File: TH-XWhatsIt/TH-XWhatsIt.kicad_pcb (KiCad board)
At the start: 2 copper layers, 162.2 x 18.8 mm, 24 parts, among them J1 BEAMSPRING CONNECTOR, J3 EXPANSION HEADER, U1 MCP4921-EP, U2 LM339, U3 74HCT595, U4 74HCT595, U5 ProMicro, U7 74HCT595

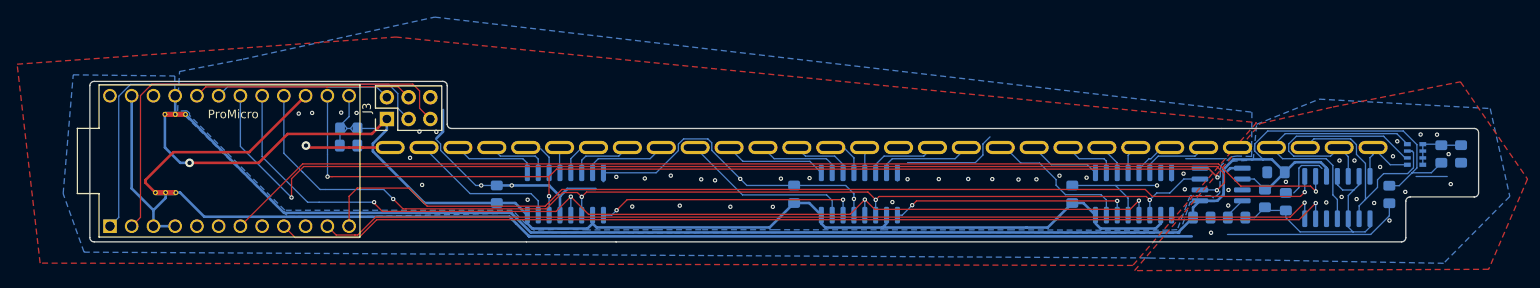
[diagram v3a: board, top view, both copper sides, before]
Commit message: cleaned up cuts in the copper fill
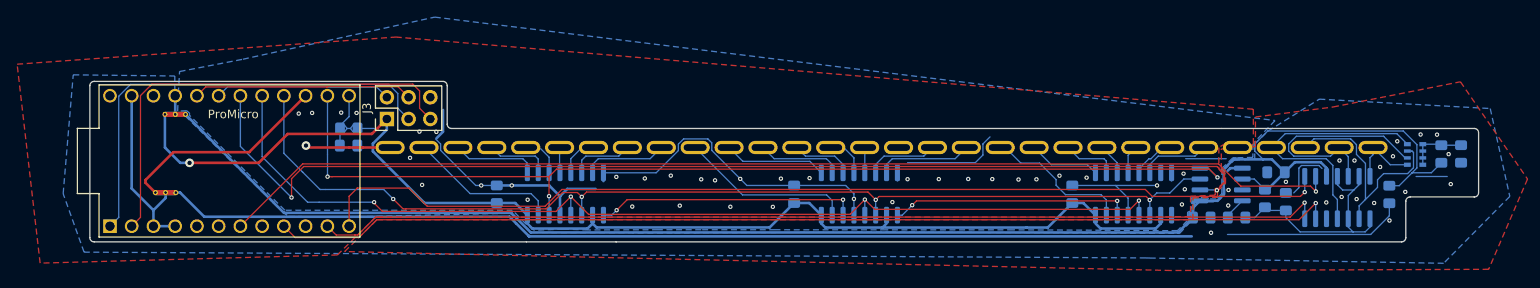
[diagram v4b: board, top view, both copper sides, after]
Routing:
- net GNDD: vias 37 -> 38
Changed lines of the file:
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@@
     (thickness 1.6)
     (drawings 20)
-    (tracks 554)
+    (tracks 555)
     (zones 0)
     (modules 24)
@@
   (layers
     (0 F.Cu jumper)
-    (31 B.Cu signal)
+    (31 B.Cu signal hide)
     (32 B.Adhes user hide)
     (33 F.Adhes user hide)
@@
     (42 Eco1.User user hide)
     (43 Eco2.User user hide)
-    (44 Edge.Cuts user hide)
+    (44 Edge.Cuts user)
     (45 Margin user hide)
     (46 B.CrtYd user hide)
@@
   (segment (start 100 153.84556) (end 100 153.524) (width 0.3048) (layer F.Cu) (net 56))
   (segment (start 101.15184 154.9974) (end 100 153.84556) (width 0.3048) (layer F.Cu) (net 56))
+  (via (at 221.09 156.38) (size 0.508) (drill 0.254) (layers F.Cu B.Cu) (net 56))
   (segment (start 103.4669 158.91662) (end 100.9269 158.91662) (width 0.3048) (layer B.Cu) (net 57))
   (segment (start 100.9269 158.91662) (end 100.9269 157.04718) (width 0.3048) (layer B.Cu) (net 57))
@@
         (xy 103.42118 141.36878) (xy 103.44404 146.00936) (xy 104.65054 146.03476) (xy 115.97386 157.22346) (xy 116.72824 157.78226)
         (xy 123.65482 157.8356) (xy 142.61084 157.4038) (xy 145.16862 159.67202) (xy 161.78276 159.70758) (xy 186.9694 159.6009)
-        (xy 220.81744 159.76092) (xy 222.0595 156.0703) (xy 225.10242 156.03474) (xy 225.8949 155.28036) (xy 225.94824 152.41778)
-        (xy 226.90328 151.33574) (xy 229.42296 151.1935) (xy 229.8192 147.0152) (xy 237.1471 144.07388) (xy 257.1115 145.17116)
-        (xy 259.3975 155.43784) (xy 251.67082 163.25088) (xy 217.42908 162.64128) (xy 216.86012 162.62604) (xy 92.8243 161.9504)
-        (xy 90.38082 155.12288) (xy 91.55684 141.23416)
+        (xy 220.81744 159.76092) (xy 222.25 158.232899) (xy 222.5 156.75442) (xy 223 156.0703) (xy 225.22 156.07)
+        (xy 226.1 155.23) (xy 226.08 152.31) (xy 227.19 151.2) (xy 229.6 151.12) (xy 229.6 149.31)
+        (xy 231.14 147.81) (xy 237.1471 144.07388) (xy 257.1115 145.17116) (xy 259.3975 155.43784) (xy 251.67082 163.25088)
+        (xy 217.42908 162.64128) (xy 216.86012 162.62604) (xy 92.8243 161.9504) (xy 90.38082 155.12288) (xy 91.55684 141.23416)
       )
     )
@@
     (polygon
       (pts
-        (xy 229.26802 145.59534) (xy 229.22992 150.76678) (xy 227.47986 150.71852) (xy 226.85502 150.81758) (xy 225.65614 151.81834)
-        (xy 225.57994 152.52446) (xy 225.51136 155.03398) (xy 224.8154 155.63342) (xy 224.52076 155.38196) (xy 222.04426 155.33624)
-        (xy 221.65818 156.3878) (xy 220.55328 159.32404) (xy 219.51188 159.37738) (xy 211.67852 159.38754) (xy 201.36358 159.34436)
-        (xy 186.53252 159.34436) (xy 173.58614 159.3342) (xy 164.93236 159.33166) (xy 159.88792 159.33166) (xy 151.72944 159.35706)
-        (xy 148.82368 159.25546) (xy 145.3896 159.39516) (xy 144.41932 158.62808) (xy 142.88262 157.05328) (xy 116.27866 157.05328)
-        (xy 111.64316 152.45588) (xy 105.11536 145.93062) (xy 105.16616 145.73504) (xy 104.81564 145.43024) (xy 103.759 145.47342)
-        (xy 103.83266 143.42364) (xy 103.98252 140.84808) (xy 111.38154 139.41298) (xy 133.79196 134.49046)
+        (xy 231.97 146.57) (xy 229.38 149.29) (xy 229.38 150.88) (xy 227.49 150.92) (xy 227.05 150.92)
+        (xy 226.24 151.71) (xy 225.84 152.08) (xy 225.76 152.23) (xy 225.75 155.13) (xy 225.09 155.74)
+        (xy 224.23 155.73) (xy 224.01 155.58) (xy 222.42 155.57) (xy 222.18 155.64) (xy 222.14 156.02)
+        (xy 222.23 156.27) (xy 222.58 156.29) (xy 222.28 156.59) (xy 222.18 156.76) (xy 222.13 157.13)
+        (xy 221.76 157.28) (xy 221.73 158.26) (xy 220.58 159.43) (xy 219.49 159.44) (xy 211.67852 159.38754)
+        (xy 201.36358 159.34436) (xy 186.53252 159.34436) (xy 173.58614 159.3342) (xy 164.93236 159.33166) (xy 159.88792 159.33166)
+        (xy 151.72944 159.35706) (xy 148.82368 159.25546) (xy 145.3896 159.39516) (xy 144.41932 158.62808) (xy 142.88262 157.05328)
+        (xy 116.27866 157.05328) (xy 111.64316 152.45588) (xy 105.11536 145.93062) (xy 105.16616 145.73504) (xy 104.81564 145.43024)
+        (xy 103.759 145.47342) (xy 103.83266 143.42364) (xy 103.98252 140.84808) (xy 111.38154 139.41298) (xy 133.79196 134.49046)
       )
     )
@@
     (polygon
       (pts
-        (xy 229.80396 146.81962) (xy 215.35898 163.50234) (xy 87.68842 163.2331) (xy 85.0011 139.9921) (xy 129.24028 136.81964)
+        (xy 229.43 145.25) (xy 229.44 149.43) (xy 226.2 149.24) (xy 225.4 149.72) (xy 225.4 152.26)
+        (xy 225.99 152.88) (xy 225.98 153.81) (xy 225.28 154.49) (xy 225.04 154.49) (xy 224.91 154.66)
+        (xy 224.97 154.88) (xy 224.99 154.98) (xy 224.98 155.29) (xy 222.1 155.43) (xy 222.1 157.8)
+        (xy 215.23 157.85) (xy 126.89 157.86) (xy 122.42 162.28) (xy 87.68842 163.2331) (xy 85.0011 139.9921)
+        (xy 129.24028 136.81964)
       )
     )
@@
     (polygon
       (pts
-        (xy 261.4676 153.40838) (xy 256.92608 163.95446) (xy 215.55202 164.1094) (xy 230.25862 146.9136) (xy 238.73968 144.99336)
-        (xy 253.62916 142.04696)
+        (xy 261.4676 153.40838) (xy 256.92608 163.95446) (xy 219.769752 164.093605) (xy 123.27 161.88) (xy 127.03 158.17)
+        (xy 222.37 158.16) (xy 222.37 155.61) (xy 225.22 155.54) (xy 225.27 154.81) (xy 226.18 153.91)
+        (xy 226.19 152.8) (xy 225.69 152.24) (xy 225.69 149.9) (xy 229.68 149.63) (xy 229.68 146.16)
+        (xy 238.73968 144.99336) (xy 253.62916 142.04696)
       )
     )

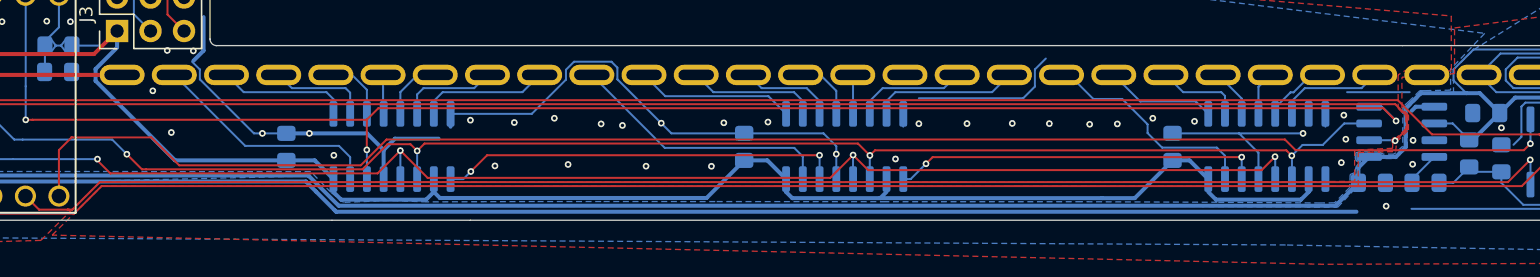
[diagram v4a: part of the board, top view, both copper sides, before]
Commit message: a bit more copper pour-related cleanups
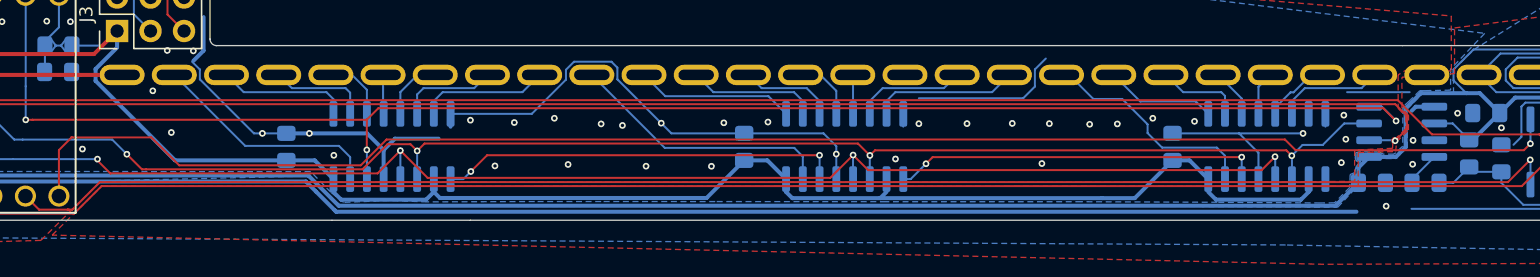
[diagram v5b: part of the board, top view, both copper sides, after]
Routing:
- net GNDD: vias 38 -> 40
- net GNDA: vias 19 -> 20
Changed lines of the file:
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@@
     (thickness 1.6)
     (drawings 20)
-    (tracks 555)
+    (tracks 558)
     (zones 0)
     (modules 24)
@@
   (layers
     (0 F.Cu jumper)
-    (31 B.Cu signal hide)
+    (31 B.Cu signal)
     (32 B.Adhes user hide)
     (33 F.Adhes user hide)
     (34 B.Paste user hide)
     (35 F.Paste user hide)
-    (36 B.SilkS user hide)
+    (36 B.SilkS user)
     (37 F.SilkS user hide)
     (38 B.Mask user hide)
@@
   (segment (start 228.14638 152.13838) (end 226.739612 152.13838) (width 0.3048) (layer B.Cu) (net 44))
   (segment (start 226.739612 152.13838) (end 226.42831 152.449682) (width 0.3048) (layer B.Cu) (net 44))
+  (via (at 229.91 152.63) (size 0.508) (drill 0.254) (layers F.Cu B.Cu) (net 44))
   (segment (start 251.71262 151.85528) (end 251.71146 151.85644) (width 0.1524) (layer B.Cu) (net 45))
   (segment (start 251.5932 151.73818) (end 251.71146 151.85644) (width 0.1524) (layer B.Cu) (net 45))
@@
   (segment (start 101.15184 154.9974) (end 100 153.84556) (width 0.3048) (layer F.Cu) (net 56))
   (via (at 221.09 156.38) (size 0.508) (drill 0.254) (layers F.Cu B.Cu) (net 56))
+  (via (at 125.57 155.35) (size 0.508) (drill 0.254) (layers F.Cu B.Cu) (net 56))
+  (via (at 198.37 156.45) (size 0.508) (drill 0.254) (layers F.Cu B.Cu) (net 56))
   (segment (start 103.4669 158.91662) (end 100.9269 158.91662) (width 0.3048) (layer B.Cu) (net 57))
   (segment (start 100.9269 158.91662) (end 100.9269 157.04718) (width 0.3048) (layer B.Cu) (net 57))

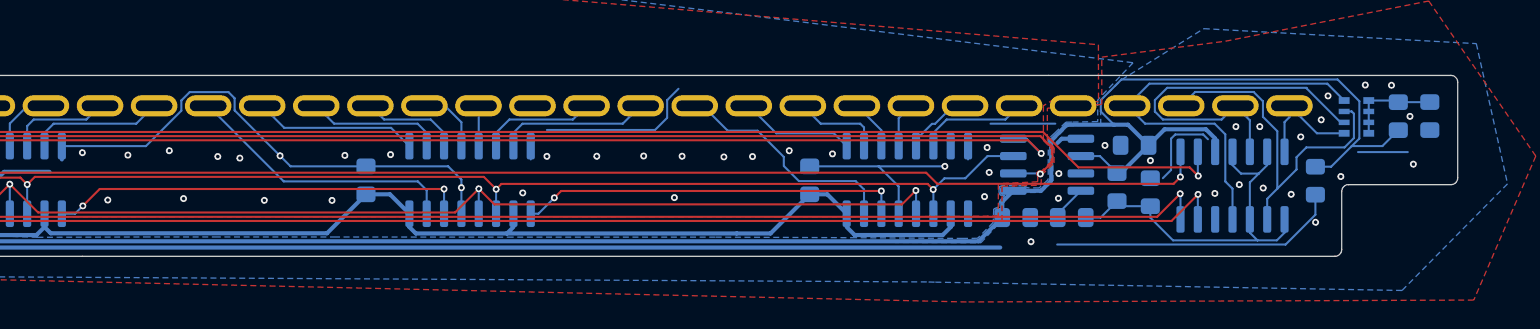
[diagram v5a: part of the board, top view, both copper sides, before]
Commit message: Added chassis ground, and added some silkscreen
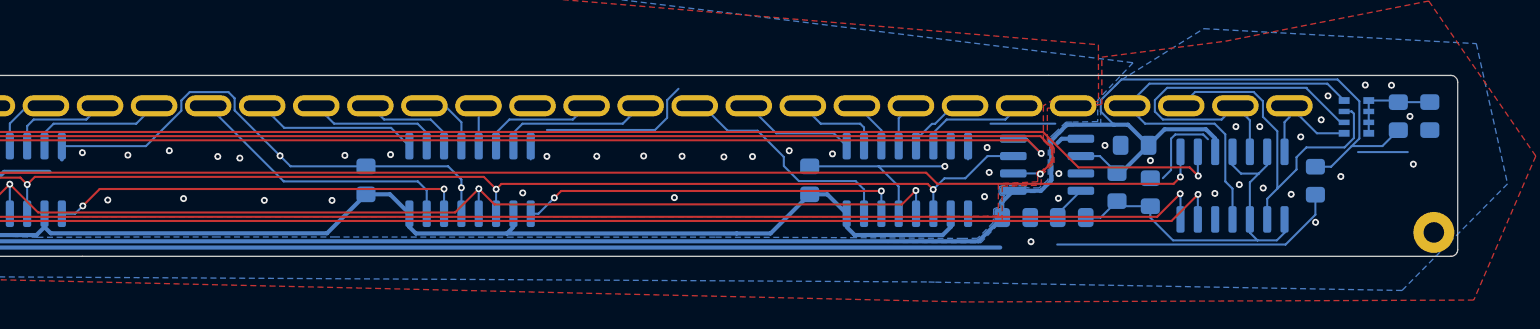
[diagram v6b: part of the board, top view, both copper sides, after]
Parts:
- added H1: MountingHole_Pad, TH-XWhatsIt:ChassisGnd, B.Cu at (254.0, 159.0)
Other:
- outline, holes or cut-outs redrawn
- board text added: "Based on original work by xwhatsit"
- board text added: "CHASSIS GND"
- board text added: "Compact-Beamspring Rev1"
- board text added: "Contributors: * pandrew * listofoptions * kmnov2017 * tentator"
- board text added: "GND"
- board text added: "RST"
